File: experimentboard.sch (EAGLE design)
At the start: 79 parts, among them IC1 TL072P, IC2 LM317, IC3 LM337, U1 PCM1690, U2 DIR9001

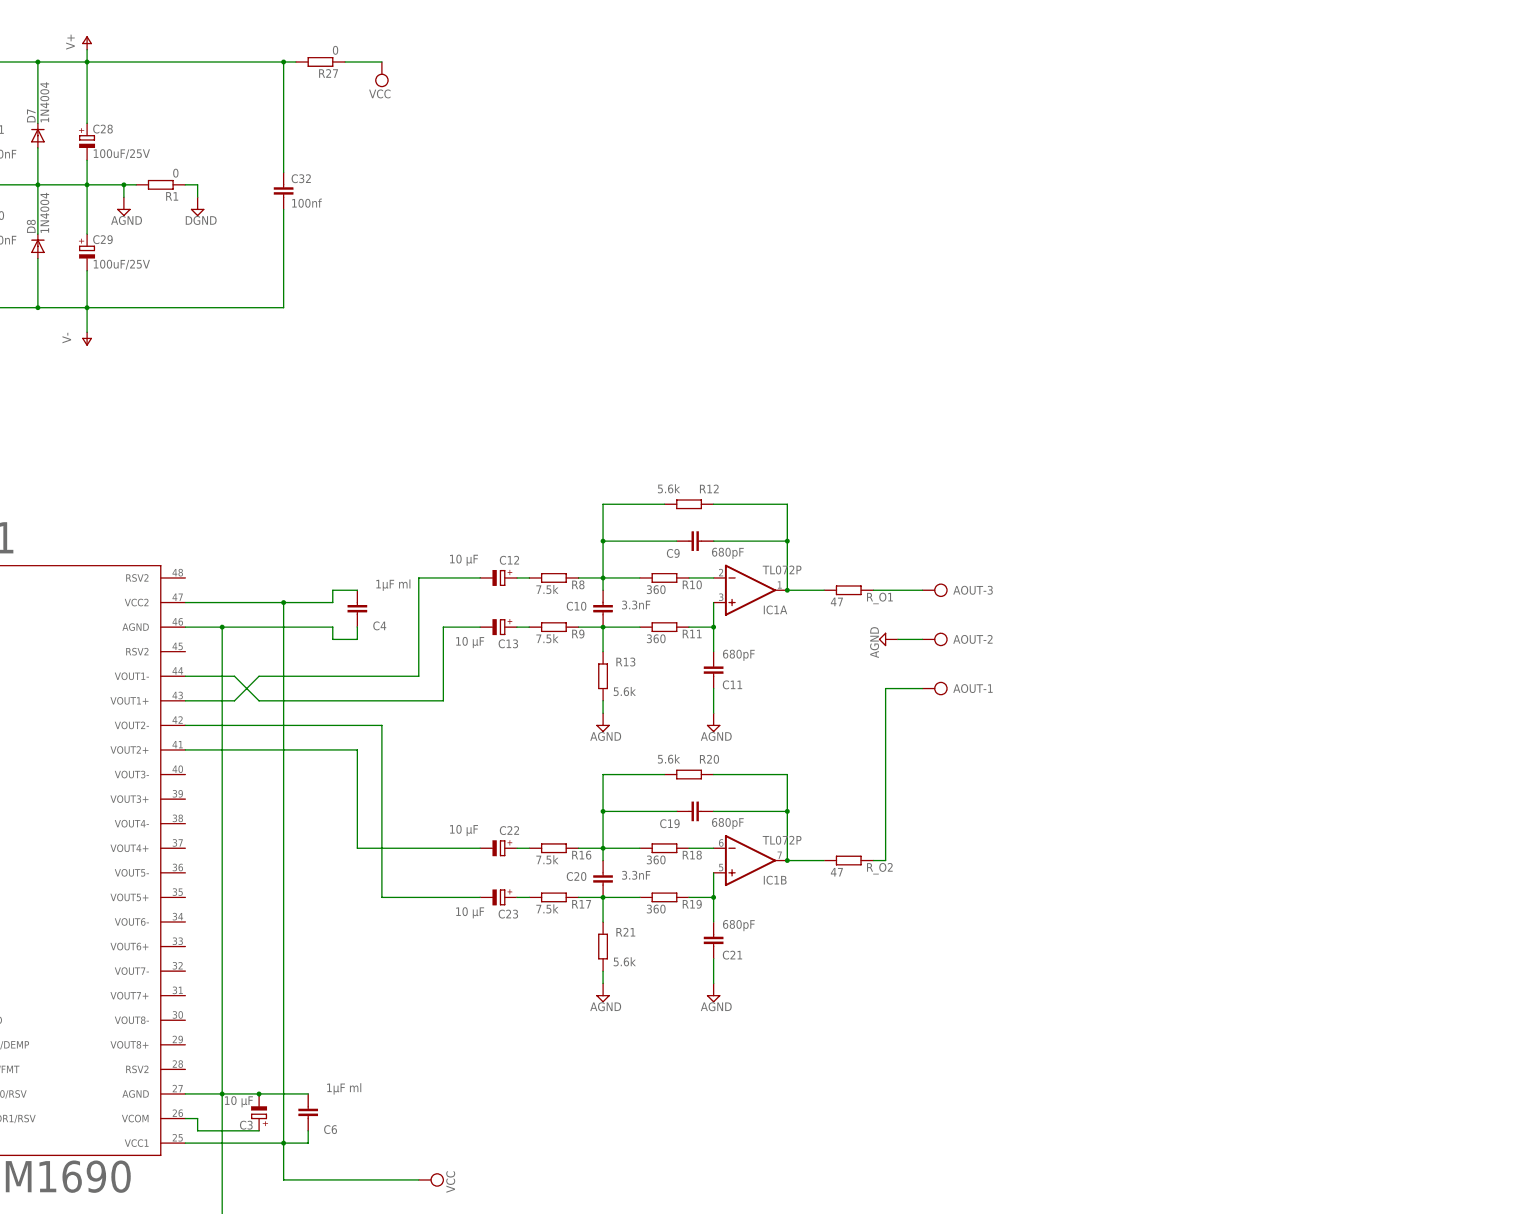
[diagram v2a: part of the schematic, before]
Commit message: Copied two extra output stages
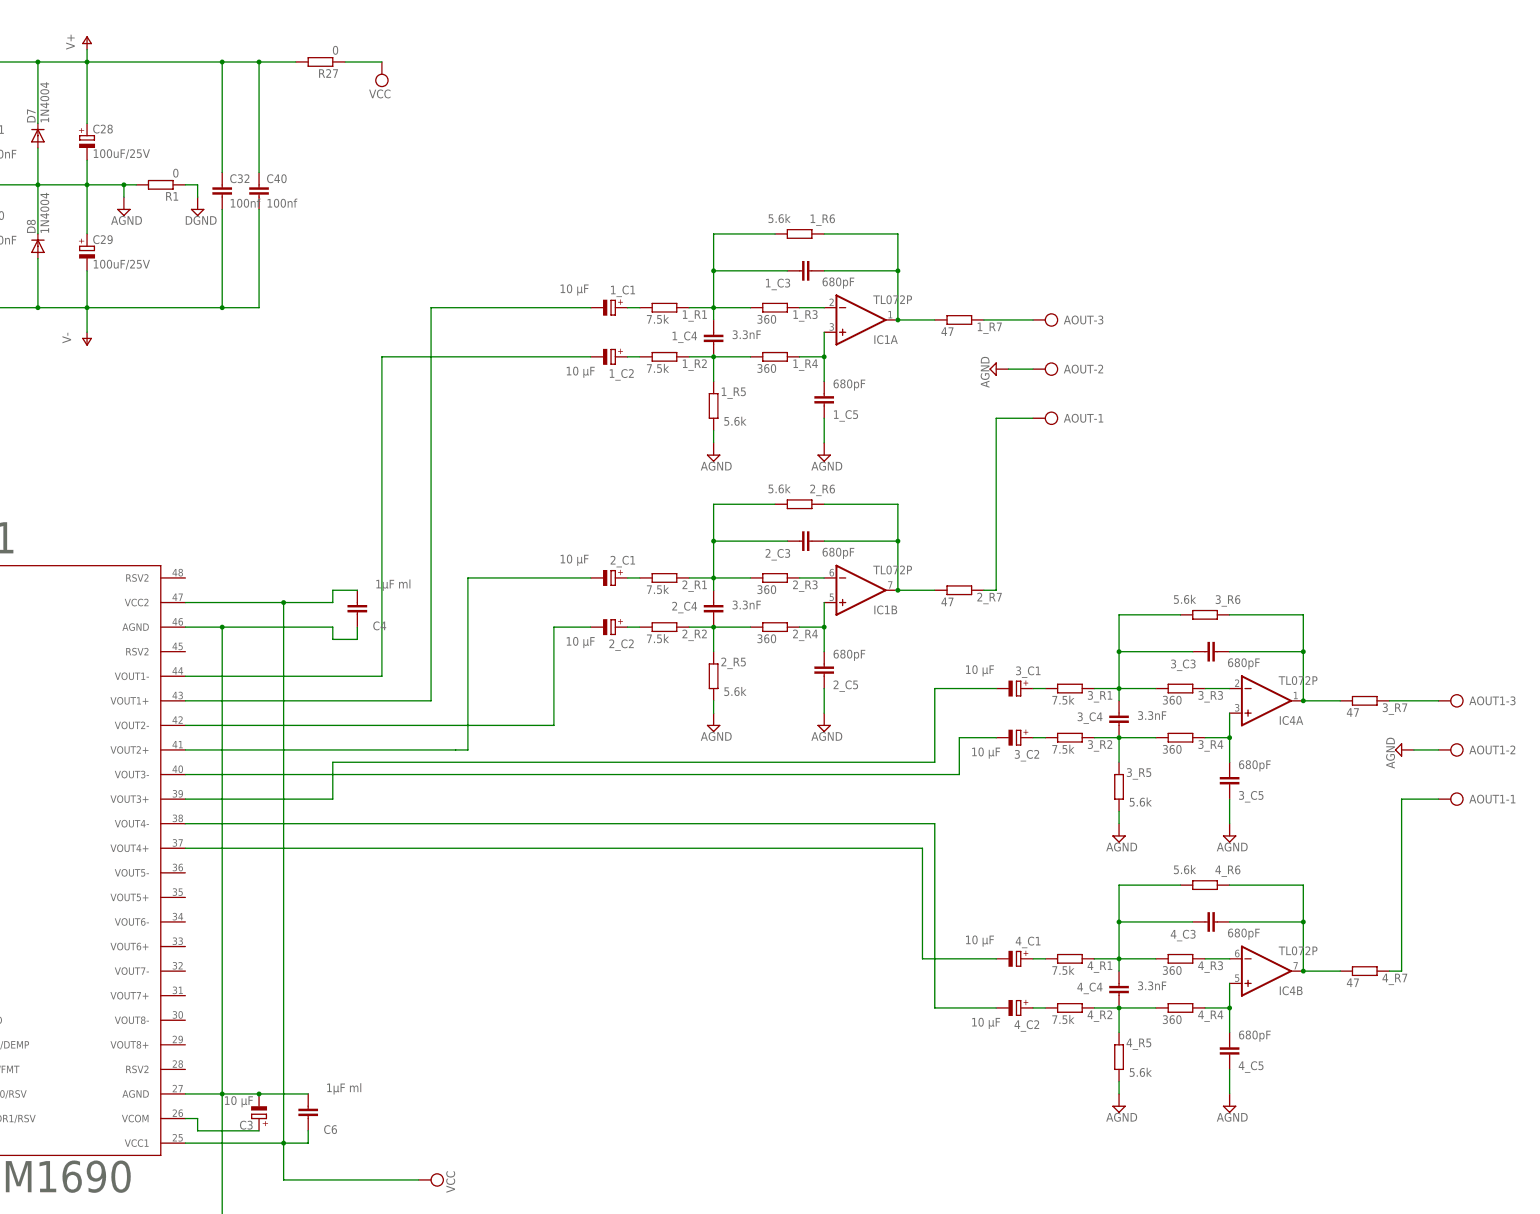
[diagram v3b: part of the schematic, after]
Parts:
- removed C10, C20: 3.3nF, rcl:C-EU050-025X075
- removed C11, C19, C21, C9: 680pF, rcl:C-EU050-024X044
- removed C12, C13, C22, C23: 10 µF, rcl:CPOL-EUE1.8-4
- removed R12, R13, R20, R21: 5.6k, rcl:R-EU_0207/7
- removed R16, R17, R8, R9: 7.5k, rcl:R-EU_0207/7
- removed R18, R19: 360, rcl:R-EU_0207/7
- removed R_O1: 47, rcl:R-EU_0207/7
- removed R_O2: 47, rcl:R-EU_0207/10
- added 1_C1, 1_C2, 2_C1, 2_C2, 3_C1, 3_C2, 4_C1, 4_C2: 10 µF, rcl:CPOL-EUE1.8-4
- added 1_C3, 1_C5, 2_C3, 2_C5, 3_C3, 3_C5, 4_C3, 4_C5: 680pF, rcl:C-EU050-024X044
- added 1_C4, 2_C4, 3_C4, 4_C4: 3.3nF, rcl:C-EU050-025X075
- added 1_R1, 1_R2, 3_R1, 3_R2, 4_R1, 4_R2: 7.5k, rcl:R-EU_0207/7
- added 1_R3, 1_R4, 2_R3, 2_R4, 3_R3, 3_R4, 4_R3, 4_R4: 360, rcl:R-EU_0207/7
- added 1_R5, 1_R6, 2_R5, 2_R6, 3_R5, 3_R6, 4_R5, 4_R6: 5.6k, rcl:R-EU_0207/7
- added 1_R7, 3_R7: 47, rcl:R-EU_0207/7
- added 2_R7, 4_R7: 47, rcl:R-EU_0207/10
- added AOUT1: (no value), con-ptr500:AK500/3
- added C40: 100nf, rcl:C-EU050-024X044
- added IC4: TL072P, 0000halfgaar:TL072P
- 2_R1, 2_R2: value 360 -> 7.5k
- renumbered R10 to 2_R1, R11 to 2_R2
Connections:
- new net N$10: 3_C3.1, 3_C4.2, 3_R1.2, 3_R3.1, 3_R6.1
- new net N$16: 3_C5.2, 3_R4.2, IC4A.+IN
- new net N$21: 3_C3.2, 3_R6.2, 3_R7.1, IC4A.OUT
- new net N$22: 3_R3.2, IC4A.-IN
- new net N$44: 3_C2.+, 3_R2.1
- new net N$45: 3_C1.+, 3_R1.1
- new net N$46: 3_C1.-, U1.VOUT3+
- new net N$47: 3_C2.-, U1.VOUT3-
- new net N$48: 4_C4.1, 4_R2.2, 4_R4.1, 4_R5.2
- new net N$49: 4_C3.1, 4_C4.2, 4_R1.2, 4_R3.1, 4_R6.1
- new net N$50: 4_C5.2, 4_R4.2, IC4B.+IN
- new net N$55: 4_C3.2, 4_R6.2, 4_R7.1, IC4B.OUT
- new net N$56: 4_R3.2, IC4B.-IN
- new net N$57: 4_C2.+, 4_R2.1
- new net N$58: 4_C1.+, 4_R1.1
- new net N$59: 4_C2.-, U1.VOUT4-
- new net N$60: 4_C1.-, U1.VOUT4+
- new net N$64: 3_R7.2, AOUT1-3.KL
- new net N$65: 4_R7.2, AOUT1-1.KL
- new net N$9: 3_C4.1, 3_R2.2, 3_R4.1, 3_R5.2
- net AGND: now also 1_C5.1, 1_R5.1, 2_C5.1, 2_R5.1, 3_C5.1, 3_R5.1, 4_C5.1, 4_R5.1, AOUT1-2.KL; no longer C11.1, C21.1, R13.1, R21.1
- net N$13: now also 1_C4.1, 1_R2.2, 1_R4.1, 1_R5.2; no longer 2_R2.1, C10.1, R13.2, R9.2
- net N$14: now also 2_C4.1, 2_R2.2, 2_R4.1, 2_R5.2; no longer C20.1, R17.2, R19.1, R21.2
- net N$15: now also 2_C3.1, 2_C4.2, 2_R1.2, 2_R3.1, 2_R6.1; no longer C19.1, C20.2, R16.2, R18.1, R20.1
- net N$18: now also 1_C3.1, 1_C4.2, 1_R1.2, 1_R3.1, 1_R6.1; no longer 2_R1.1, C10.2, C9.1, R12.1, R8.2
- net N$23: now also 1_R3.2; no longer 2_R1.2
- net N$24: now also 1_C5.2, 1_R4.2; no longer 2_R2.2, C11.2
- net N$25: now also 1_C2.+, 1_R2.1; no longer C13.+, R9.1
- net N$26: now also 1_C3.2, 1_R6.2, 1_R7.1; no longer C9.2, R12.2, R_O1.1
- net N$27: now also 1_C1.+, 1_R1.1; no longer C12.+, R8.1
- net N$28: now also 1_C1.-; no longer C12.-
- net N$29: now also 1_C2.-; no longer C13.-
- net N$30: now also 2_C5.2, 2_R4.2; no longer C21.2, R19.2
- net N$31: now also 2_C3.2, 2_R6.2, 2_R7.1; no longer C19.2, R20.2, R_O2.1
- net N$32: now also 2_R3.2; no longer R18.2
- net N$33: now also 2_C2.+, 2_R2.1; no longer C23.+, R17.1
- net N$34: now also 2_C1.+, 2_R1.1; no longer C22.+, R16.1
- net N$35: now also 2_C2.-; no longer C23.-
- net N$36: now also 2_C1.-; no longer C22.-
- net N$37: now also 1_R7.2; no longer R_O1.2
- net N$38: now also 2_R7.2; no longer R_O2.2
- net V+: now also C40.1
- net V-: now also C40.2
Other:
- moved on the sheet: AOUT-1, AOUT-2, AOUT-3, C32, IC1A, IC1B

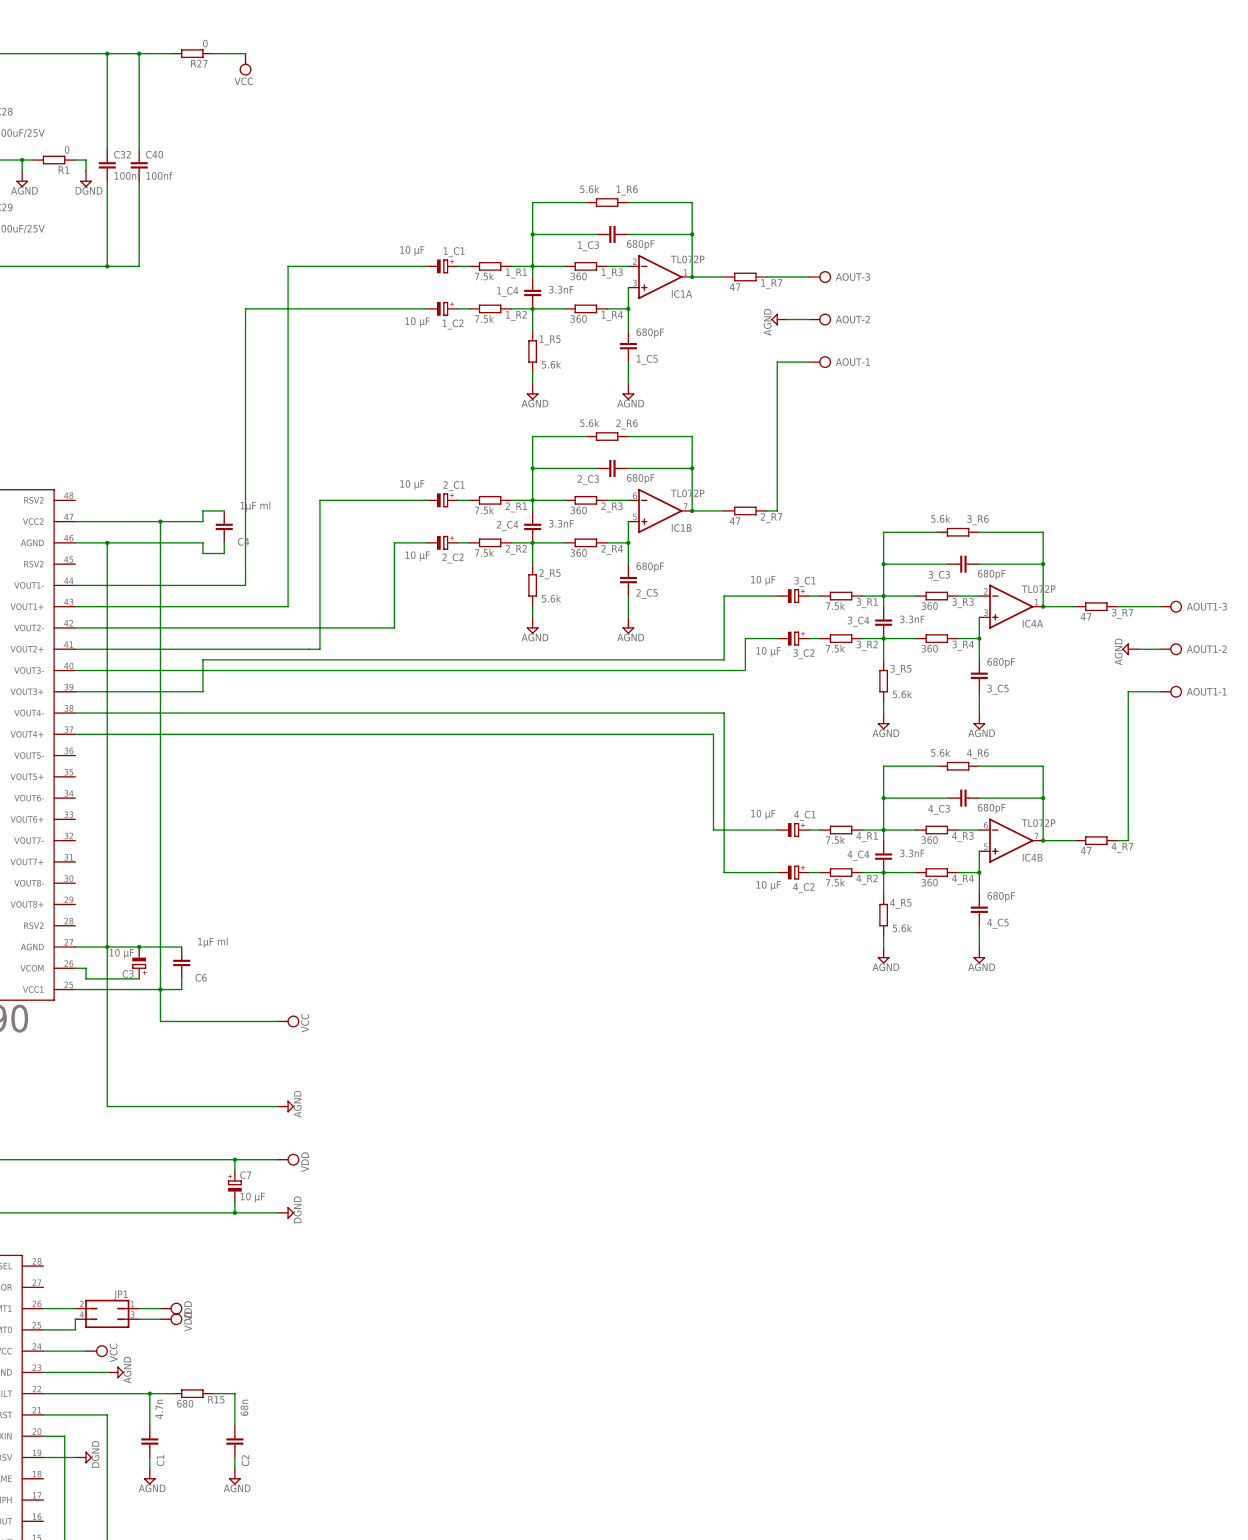
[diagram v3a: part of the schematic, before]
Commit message: Added another analog output stage
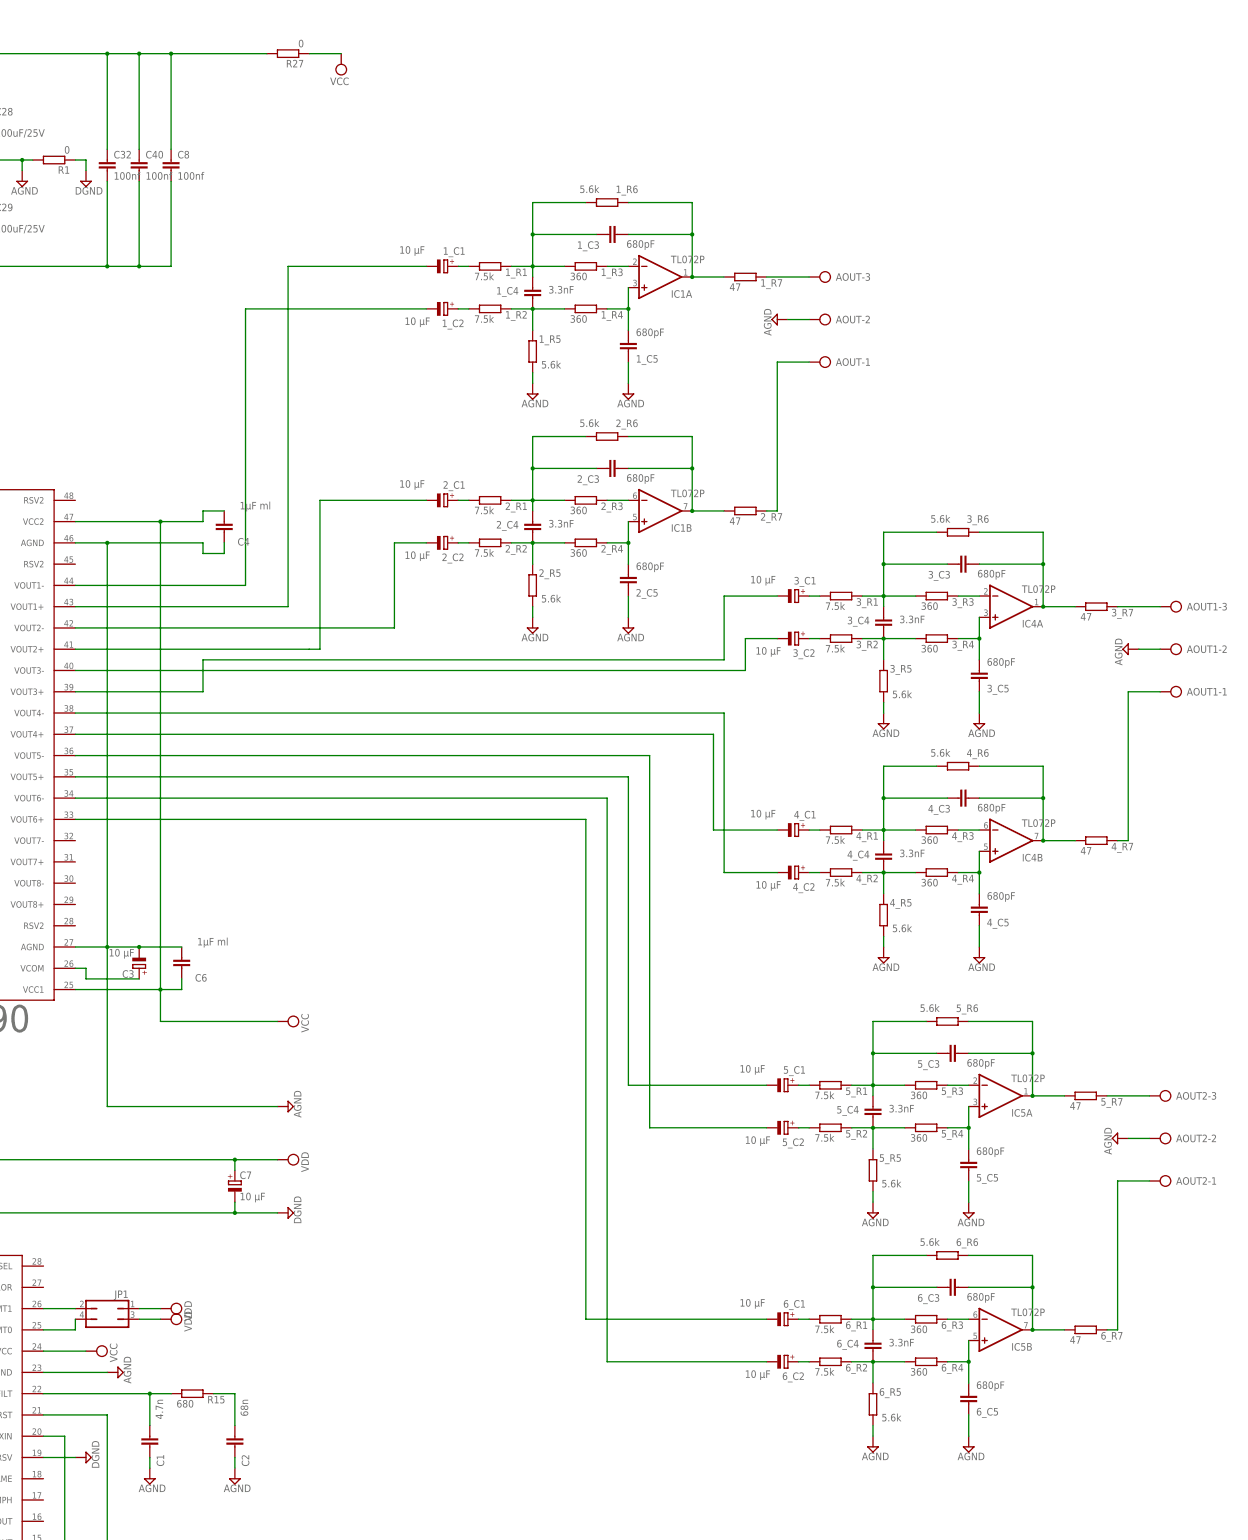
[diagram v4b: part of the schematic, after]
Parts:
- added 5_C1, 5_C2, 6_C1, 6_C2: 10 µF, rcl:CPOL-EUE1.8-4
- added 5_C3, 5_C5, 6_C3, 6_C5: 680pF, rcl:C-EU050-024X044
- added 5_C4, 6_C4: 3.3nF, rcl:C-EU050-025X075
- added 5_R1, 5_R2, 6_R1, 6_R2: 7.5k, rcl:R-EU_0207/7
- added 5_R3, 5_R4, 6_R3, 6_R4: 360, rcl:R-EU_0207/7
- added 5_R5, 5_R6, 6_R5, 6_R6: 5.6k, rcl:R-EU_0207/7
- added 5_R7: 47, rcl:R-EU_0207/7
- added 6_R7: 47, rcl:R-EU_0207/10
- added AOUT2: (no value), con-ptr500:AK500/3
- added C8: 100nf, rcl:C-EU050-024X044
- added IC5: TL072P, 0000halfgaar:TL072P
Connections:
- net N$28 renamed VOUT1+
- net N$29 renamed VOUT1-
- net N$35 renamed VOUT2-
- net N$36 renamed VOUT2+
- net N$46 renamed VOUT3+
- net N$47 renamed VOUT3-
- net N$59 renamed VOUT4-
- net N$60 renamed VOUT4+
- new net N$66: 5_C4.1, 5_R2.2, 5_R4.1, 5_R5.2
- new net N$67: 5_C3.1, 5_C4.2, 5_R1.2, 5_R3.1, 5_R6.1
- new net N$68: 5_C5.2, 5_R4.2, IC5A.+IN
- new net N$69: 5_C3.2, 5_R6.2, 5_R7.1, IC5A.OUT
- new net N$70: 5_R3.2, IC5A.-IN
- new net N$71: 5_C2.+, 5_R2.1
- new net N$72: 5_C1.+, 5_R1.1
- new net N$75: 6_C4.1, 6_R2.2, 6_R4.1, 6_R5.2
- new net N$76: 6_C3.1, 6_C4.2, 6_R1.2, 6_R3.1, 6_R6.1
- new net N$77: 6_C5.2, 6_R4.2, IC5B.+IN
- new net N$78: 6_C3.2, 6_R6.2, 6_R7.1, IC5B.OUT
- new net N$79: 6_R3.2, IC5B.-IN
- new net N$80: 6_C2.+, 6_R2.1
- new net N$81: 6_C1.+, 6_R1.1
- new net N$82: 5_R7.2, AOUT2-3.KL
- new net N$83: 6_R7.2, AOUT2-1.KL
- new net VOUT5+: 5_C1.-, U1.VOUT5+
- new net VOUT5-: 5_C2.-, U1.VOUT5-
- new net VOUT6+: 6_C1.-, U1.VOUT6+
- new net VOUT6-: 6_C2.-, U1.VOUT6-
- net AGND: now also 5_C5.1, 5_R5.1, 6_C5.1, 6_R5.1, AOUT2-2.KL
- net V+: now also C8.1
- net V-: now also C8.2
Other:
- moved on the sheet: R27

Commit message: Added the last analog output stage
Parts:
- added 7_C1, 7_C2, 8_C1, 8_C2: 10 µF, rcl:CPOL-EUE1.8-4
- added 7_C3, 7_C5, 8_C3, 8_C5: 680pF, rcl:C-EU050-024X044
- added 7_C4, 8_C4: 3.3nF, rcl:C-EU050-025X075
- added 7_R1, 7_R2, 8_R1, 8_R2: 7.5k, rcl:R-EU_0207/7
- added 7_R3, 7_R4, 8_R3, 8_R4: 360, rcl:R-EU_0207/7
- added 7_R5, 7_R6, 8_R5, 8_R6: 5.6k, rcl:R-EU_0207/7
- added 7_R7: 47, rcl:R-EU_0207/7
- added 8_R7: 47, rcl:R-EU_0207/10
- added AOUT3: (no value), con-ptr500:AK500/3
- added C9: 100nf, rcl:C-EU050-024X044
- added IC6: TL072P, 0000halfgaar:TL072P
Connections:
- new net N$29: 7_C4.1, 7_R2.2, 7_R4.1, 7_R5.2
- new net N$35: 7_C3.1, 7_C4.2, 7_R1.2, 7_R3.1, 7_R6.1
- new net N$36: 7_C5.2, 7_R4.2, IC6A.+IN
- new net N$46: 7_C3.2, 7_R6.2, 7_R7.1, IC6A.OUT
- new net N$47: 7_R3.2, IC6A.-IN
- new net N$59: 7_C2.+, 7_R2.1
- new net N$60: 7_C1.+, 7_R1.1
- new net N$73: 8_C4.1, 8_R2.2, 8_R4.1, 8_R5.2
- new net N$74: 8_C3.1, 8_C4.2, 8_R1.2, 8_R3.1, 8_R6.1
- new net N$84: 8_C5.2, 8_R4.2, IC6B.+IN
- new net N$85: 8_C3.2, 8_R6.2, 8_R7.1, IC6B.OUT
- new net N$86: 8_R3.2, IC6B.-IN
- new net N$87: 8_C2.+, 8_R2.1
- new net N$88: 8_C1.+, 8_R1.1
- new net N$89: 7_R7.2, AOUT3-3.KL
- new net N$90: 8_R7.2, AOUT3-1.KL
- new net VOUT7+: 7_C1.-, U1.VOUT7+
- new net VOUT7-: 7_C2.-, U1.VOUT7-
- new net VOUT8+: 8_C1.-, U1.VOUT8+
- new net VOUT8-: 8_C2.-, U1.VOUT8-
- net AGND: now also 7_C5.1, 7_R5.1, 8_C5.1, 8_R5.1, AOUT3-2.KL
- net V+: now also C9.1
- net V-: now also C9.2

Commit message: Working on EEPROM and TOSLINK
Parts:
- added C10, C11: 100nf, rcl:C-EU050-024X044
- added L1: 47uH, rcl:L-EU0207/10
- added R2, R8, R9: 5.6k, rcl:R-EU_0207/7
- added U$1: PLR135/T9, 0000halfgaar:PLR135/T9
- added U3: CAT24C256, 0000halfgaar:CAT24C256
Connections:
- new net CAPE_I2C_SCL: R8.1, U$2.EEPROM_I2C_SCL, U3.SCL
- new net CAPE_I2C_SDA: R2.1, U$2.EEPROM_I2C_SDA, U3.SDA
- net DGND: now also C10.1, C11.1, U$1.GND, U3.VSS
- net N$20: now also U$1.OUT
- net N$54: now also R9.1, U3.A2; no longer U2.SCKO
- net VDD: now also C10.2, C11.2, L1.1, L1.2, R2.2, R8.2, R9.2, U$1.VDD, U3.VCC
